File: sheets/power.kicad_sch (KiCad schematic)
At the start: 85 parts, among them Q11 C1815, Q12 A1015, Q13 A1442, T1 COIL, U11 74LS05, U12 74LS06, U28 PC4741, U29 PC4741, U33 74AS04, U37 LM2576T-5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

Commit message: Update Power Circuit 9
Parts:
- added R83: 100, 1_NeoGeoLibrary:CAP3-5mm, symbol Device:R_Small
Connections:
- net GND: now also R83.2; no longer D12.1 (K)
- net VCC: now also D12.1 (K)
- net at Q12.2 (C), Q13.1 (B): now also R83.1
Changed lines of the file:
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@@
   (junction (at 140.335 127) (diameter 0) (color 0 0 0 0)
+  )
+  (junction (at 85.09 74.93) (diameter 0) (color 0 0 0 0)
   )
   (junction (at 160.782 141.605) (diameter 0) (color 0 0 0 0)
@@
     (stroke (width 0) (type default) (color 0 0 0 0))
   )
-  (wire (pts (xy 108.966 106.68) (xy 108.966 107.569))
+  (wire (pts (xy 108.966 106.68) (xy 108.966 108.458))
     (stroke (width 0) (type default) (color 0 0 0 0))
   )
@@
     (stroke (width 0) (type default) (color 0 0 0 0))
   )
-  (wire (pts (xy 82.55 74.93) (xy 87.884 74.93))
+  (wire (pts (xy 82.55 74.93) (xy 85.09 74.93))
     (stroke (width 0) (type default) (color 0 0 0 0))
   )
@@
     (stroke (width 0) (type default) (color 0 0 0 0))
   )
+  (wire (pts (xy 85.09 74.93) (xy 87.884 74.93))
+    (stroke (width 0) (type default) (color 0 0 0 0))
+  )
   (wire (pts (xy 140.462 146.685) (xy 150.622 146.685))
     (stroke (width 0) (type default) (color 0 0 0 0))
@@
   )
   (wire (pts (xy 140.589 60.706) (xy 158.623 60.706))
+    (stroke (width 0) (type default) (color 0 0 0 0))
+  )
+  (wire (pts (xy 85.09 74.93) (xy 85.09 75.184))
     (stroke (width 0) (type default) (color 0 0 0 0))
   )
@@
     (pin "1")
   )
+  (symbol (lib_id "Device:R_Small") (at 85.09 77.724 0) (mirror y) (unit 1)
+    (in_bom yes) (on_board yes)
+    (property "Reference" "R83" (id 0) (at 88.011 76.581 0))
+    (property "Value" "100" (id 1) (at 88.011 78.867 0))
+    (property "Footprint" "1_NeoGeoLibrary:CAP3-5mm" (id 2) (at 85.09 77.724 0)
+      (effects (font (size 1.27 1.27)) hide)
+    )
+    (property "Datasheet" "~" (id 3) (at 85.09 77.724 0)
+      (effects (font (size 1.27 1.27)) hide)
+    )
+    (pin "1")
+    (pin "2")
+  )
   (symbol (lib_id "74xx:74LS04") (at 30.48 218.44 0) (unit 1)
     (in_bom yes) (on_board yes)
@@
     (pin "1")
   )
+  (symbol (lib_id "power:GND") (at 85.09 80.264 0) (unit 1)
+    (in_bom yes) (on_board yes)
+    (property "Reference" "#PWR?" (id 0) (at 85.09 86.614 0)
+      (effects (font (size 1.27 1.27)) hide)
+    )
+    (property "Value" "GND" (id 1) (at 85.09 83.82 0))
+    (property "Footprint" "" (id 2) (at 85.09 80.264 0)
+      (effects (font (size 1.27 1.27)) hide)
+    )
+    (property "Datasheet" "" (id 3) (at 85.09 80.264 0)
+      (effects (font (size 1.27 1.27)) hide)
+    )
+    (pin "1")
+  )
   (symbol (lib_id "power:GND") (at 140.589 70.866 0) (unit 1)
     (in_bom yes) (on_board yes)
@@
     )
     (property "Datasheet" "" (id 3) (at 23.368 271.78 0)
+      (effects (font (size 1.27 1.27)) hide)
+    )
+    (pin "1")
+  )
+  (symbol (lib_id "power:VCC") (at 108.966 108.458 180) (unit 1)
+    (in_bom yes) (on_board yes)
+    (property "Reference" "#PWR?" (id 0) (at 108.966 104.648 0)
+      (effects (font (size 1.27 1.27)) hide)
+    )
+    (property "Value" "VCC" (id 1) (at 108.966 112.268 0))
+    (property "Footprint" "" (id 2) (at 108.966 108.458 0)
+      (effects (font (size 1.27 1.27)) hide)
+    )
+    (property "Datasheet" "" (id 3) (at 108.966 108.458 0)
       (effects (font (size 1.27 1.27)) hide)
     )
@@
     (pin "2")
   )
-  (symbol (lib_id "power:GND") (at 108.966 107.569 0) (unit 1)
-    (in_bom yes) (on_board yes) (fields_autoplaced)
-    (property "Reference" "#PWR0279" (id 0) (at 108.966 113.919 0)
-      (effects (font (size 1.27 1.27)) hide)
-    )
-    (property "Value" "GND" (id 1) (at 108.966 112.395 0))
-    (property "Footprint" "" (id 2) (at 108.966 107.569 0)
-      (effects (font (size 1.27 1.27)) hide)
-    )
-    (property "Datasheet" "" (id 3) (at 108.966 107.569 0)
-      (effects (font (size 1.27 1.27)) hide)
-    )
-    (pin "1")
-  )
   (symbol (lib_id "74xx:74LS04") (at 30.48 187.96 0) (unit 3)

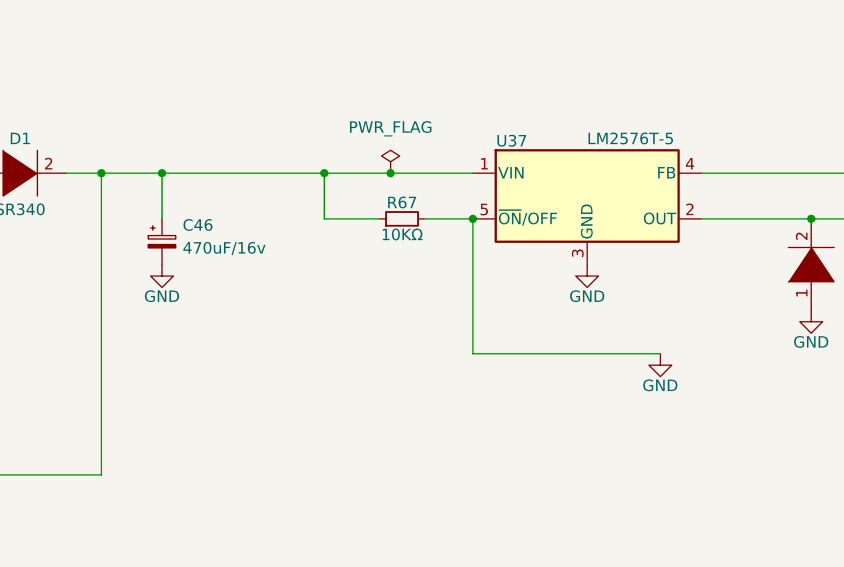
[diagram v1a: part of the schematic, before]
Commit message: Update Power Circuit 10
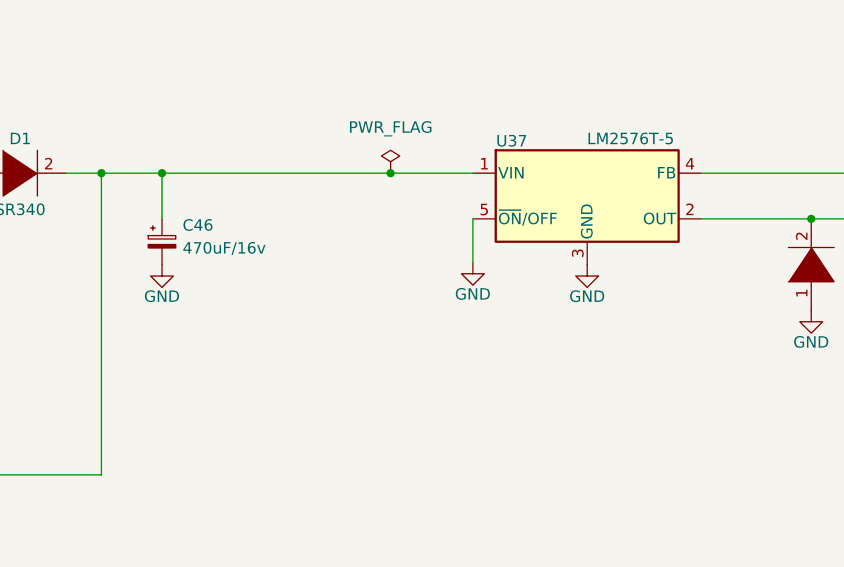
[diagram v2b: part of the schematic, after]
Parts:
- removed R67: 10KΩ, 1_NeoGeoLibrary:Resistor1-5mm, symbol Device:R_Small
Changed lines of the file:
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@@
   (junction (at 48.895 127) (diameter 0) (color 0 0 0 0)
   )
-  (junction (at 158.623 60.706) (diameter 0) (color 0 0 0 0)
-  )
   (junction (at 191.262 146.685) (diameter 0) (color 0 0 0 0)
   )
@@
   )
   (junction (at 23.368 246.38) (diameter 0) (color 0 0 0 0)
-  )
-  (junction (at 175.133 65.786) (diameter 0) (color 0 0 0 0)
   )
   (junction (at 89.535 127) (diameter 0) (color 0 0 0 0)
@@
     (stroke (width 0) (type default) (color 0 0 0 0))
   )
-  (wire (pts (xy 169.799 65.786) (xy 175.133 65.786))
-    (stroke (width 0) (type default) (color 0 0 0 0))
-  )
-  (wire (pts (xy 175.133 80.772) (xy 195.961 80.772))
-    (stroke (width 0) (type default) (color 0 0 0 0))
-  )
   (wire (pts (xy 252.222 141.605) (xy 262.382 141.605))
     (stroke (width 0) (type default) (color 0 0 0 0))
@@
     (stroke (width 0) (type default) (color 0 0 0 0))
   )
-  (wire (pts (xy 158.623 65.786) (xy 164.719 65.786))
-    (stroke (width 0) (type default) (color 0 0 0 0))
-  )
   (wire (pts (xy 59.182 146.685) (xy 69.342 146.685))
     (stroke (width 0) (type default) (color 0 0 0 0))
@@
     (stroke (width 0) (type default) (color 0 0 0 0))
   )
-  (wire (pts (xy 158.623 60.706) (xy 165.989 60.706))
-    (stroke (width 0) (type default) (color 0 0 0 0))
-  )
   (wire (pts (xy 49.022 141.605) (xy 59.182 141.605))
     (stroke (width 0) (type default) (color 0 0 0 0))
@@
     (stroke (width 0) (type default) (color 0 0 0 0))
   )
+  (wire (pts (xy 175.133 65.786) (xy 175.133 70.612))
+    (stroke (width 0) (type default) (color 0 0 0 0))
+  )
   (wire (pts (xy 22.86 218.44) (xy 22.86 223.52))
     (stroke (width 0) (type default) (color 0 0 0 0))
   )
-  (wire (pts (xy 175.133 65.786) (xy 175.133 80.772))
-    (stroke (width 0) (type default) (color 0 0 0 0))
-  )
   (wire (pts (xy 256.413 65.786) (xy 262.001 65.786))
     (stroke (width 0) (type default) (color 0 0 0 0))
@@
     (stroke (width 0) (type default) (color 0 0 0 0))
   )
-  (wire (pts (xy 158.623 60.706) (xy 158.623 65.786))
-    (stroke (width 0) (type default) (color 0 0 0 0))
-  )
   (wire (pts (xy 241.935 132.08) (xy 252.095 132.08))
     (stroke (width 0) (type default) (color 0 0 0 0))
@@
     (stroke (width 0) (type default) (color 0 0 0 0))
   )
-  (wire (pts (xy 140.589 60.706) (xy 158.623 60.706))
+  (wire (pts (xy 140.589 60.706) (xy 165.989 60.706))
     (stroke (width 0) (type default) (color 0 0 0 0))
   )
@@
     (pin "2")
   )
-  (symbol (lib_id "power:GND") (at 195.961 80.772 0) (unit 1)
-    (in_bom yes) (on_board yes)
-    (property "Reference" "#PWR0258" (id 0) (at 195.961 87.122 0)
-      (effects (font (size 1.27 1.27)) hide)
-    )
-    (property "Value" "GND" (id 1) (at 195.961 84.328 0))
-    (property "Footprint" "" (id 2) (at 195.961 80.772 0)
-      (effects (font (size 1.27 1.27)) hide)
-    )
-    (property "Datasheet" "" (id 3) (at 195.961 80.772 0)
+  (symbol (lib_id "power:GND") (at 175.133 70.612 0) (unit 1)
+    (in_bom yes) (on_board yes)
+    (property "Reference" "#PWR0258" (id 0) (at 175.133 76.962 0)
+      (effects (font (size 1.27 1.27)) hide)
+    )
+    (property "Value" "GND" (id 1) (at 175.133 74.168 0))
+    (property "Footprint" "" (id 2) (at 175.133 70.612 0)
+      (effects (font (size 1.27 1.27)) hide)
+    )
+    (property "Datasheet" "" (id 3) (at 175.133 70.612 0)
       (effects (font (size 1.27 1.27)) hide)
     )
@@
       (effects (font (size 1.27 1.27)) hide)
     )
-    (pin "1")
-    (pin "2")
-  )
-  (symbol (lib_id "Device:R_Small") (at 167.259 65.786 90) (unit 1)
-    (in_bom yes) (on_board yes)
-    (property "Reference" "R67" (id 0) (at 167.259 64.008 90))
-    (property "Value" "10KΩ" (id 1) (at 167.259 67.564 90))
-    (property "Footprint" "1_NeoGeoLibrary:Resistor1-5mm" (id 2) (at 167.259 65.786 0)
-      (effects (font (size 1.27 1.27)) hide)
-    )
-    (property "Datasheet" "" (id 3) (at 167.259 65.786 0)
-      (effects (font (size 1.27 1.27)) hide)
-    )

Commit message: Merged From Stable
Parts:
- C126: footprint 1_NeoGeoLibrary:CAP3-5mm -> 1_NeoGeoLibrary:CAP2-2.5mm
- C44, C45: footprint 1_NeoGeoLibrary:CAP1-5mm -> 1_NeoGeoLibrary:CAP3-5mm
- C46: footprint 1_NeoGeoLibrary:CAP3-5mm -> 1_NeoGeoLibrary:CAP1-5mm
- C47: footprint 1_NeoGeoLibrary:CAP3-5mm -> 1_NeoGeoLibrary:CAP4-Large
- D1, D2: footprint Diode_THT:D_A-405_P10.16mm_Horizontal -> Diode_THT:D_DO-15_P15.24mm_Horizontal
- D11, D12: footprint Diode_THT:D_A-405_P10.16mm_Horizontal -> Diode_THT:D_A-405_P7.62mm_Horizontal
- J4: footprint Jumper:SolderJumper-2_P1.3mm_Open_Pad1.0x1.5mm -> 1_NeoGeoLibrary:J4
- L3: footprint 1_NeoGeoLibrary:Resistor1-5mm -> Inductor_THT:L_Toroid_Vertical_L35.1mm_W21.1mm_P18.50mm_Vishay_TJ6
- Q11: footprint Package_TO_SOT_THT:TO-92_Inline -> Package_TO_SOT_THT:TO-92_Inline_Wide
- Q13: footprint Package_TO_SOT_THT:TO-3P-3_Vertical -> Package_TO_SOT_THT:TO-220-3_Vertical
- R77: footprint 1_NeoGeoLibrary:CAP3-5mm -> Resistor_THT:R_Axial_DIN0309_L9.0mm_D3.2mm_P25.40mm_Horizontal
- R78, R79, R80, R81, R82: footprint 1_NeoGeoLibrary:CAP3-5mm -> Resistor_THT:R_Axial_DIN0207_L6.3mm_D2.5mm_P10.16mm_Horizontal
- R83: footprint 1_NeoGeoLibrary:CAP3-5mm -> Resistor_THT:R_Axial_DIN0309_L9.0mm_D3.2mm_P20.32mm_Horizontal
- SW2: footprint Button_Switch_THT:SW_Slide_1P2T_CK_OS102011MS2Q -> 1_NeoGeoLibrary:SW2
- T1: footprint Transformer_THT:Transformer_NF_ETAL_1-1_P1200 -> 1_NeoGeoLibrary:T1
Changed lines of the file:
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@@
     (property "Reference" "J4" (id 0) (at 29.718 16.0528 90))
     (property "Value" "~" (id 1) (at 30.0736 16.1036 90))
-    (property "Footprint" "Jumper:SolderJumper-2_P1.3mm_Open_Pad1.0x1.5mm" (id 2) (at 30.734 23.622 0)
+    (property "Footprint" "1_NeoGeoLibrary:J4" (id 2) (at 30.734 23.622 0)
       (effects (font (size 1.27 1.27)) hide)
     )
@@
       (effects (font (size 1.27 1.27)) (justify left))
     )
-    (property "Footprint" "Package_TO_SOT_THT:TO-3P-3_Vertical" (id 2) (at 98.044 77.47 0)
+    (property "Footprint" "Package_TO_SOT_THT:TO-220-3_Vertical" (id 2) (at 98.044 77.47 0)
       (effects (font (size 1.27 1.27)) hide)
     )
@@
     (property "Reference" "R81" (id 0) (at 111.887 73.533 0))
     (property "Value" "100" (id 1) (at 111.887 75.819 0))
-    (property "Footprint" "1_NeoGeoLibrary:CAP3-5mm" (id 2) (at 108.966 74.676 0)
+    (property "Footprint" "Resistor_THT:R_Axial_DIN0207_L6.3mm_D2.5mm_P10.16mm_Horizontal" (id 2) (at 108.966 74.676 0)
       (effects (font (size 1.27 1.27)) hide)
     )
@@
       (effects (font (size 1.27 1.27)) (justify right))
     )
-    (property "Footprint" "Diode_THT:D_A-405_P10.16mm_Horizontal" (id 2) (at 108.966 104.14 90)
+    (property "Footprint" "Diode_THT:D_A-405_P7.62mm_Horizontal" (id 2) (at 108.966 104.14 90)
       (effects (font (size 1.27 1.27)) hide)
     )
@@
     (property "Reference" "R80" (id 0) (at 46.355 78.994 0))
     (property "Value" "470" (id 1) (at 46.355 81.28 0))
-    (property "Footprint" "1_NeoGeoLibrary:CAP3-5mm" (id 2) (at 49.276 80.137 0)
+    (property "Footprint" "Resistor_THT:R_Axial_DIN0207_L6.3mm_D2.5mm_P10.16mm_Horizontal" (id 2) (at 49.276 80.137 0)
       (effects (font (size 1.27 1.27)) hide)
     )
@@
     (property "Reference" "R83" (id 0) (at 88.011 76.581 0))
     (property "Value" "100" (id 1) (at 88.011 78.867 0))
-    (property "Footprint" "1_NeoGeoLibrary:CAP3-5mm" (id 2) (at 85.09 77.724 0)
+    (property "Footprint" "Resistor_THT:R_Axial_DIN0309_L9.0mm_D3.2mm_P20.32mm_Horizontal" (id 2) (at 85.09 77.724 0)
       (effects (font (size 1.27 1.27)) hide)
     )
@@
       (effects (font (size 1.27 1.27)) (justify left))
     )
-    (property "Footprint" "1_NeoGeoLibrary:CAP3-5mm" (id 2) (at 18.542 144.145 0)
+    (property "Footprint" "1_NeoGeoLibrary:CAP2-2.5mm" (id 2) (at 18.542 144.145 0)
       (effects (font (size 1.27 1.27)) hide)
     )
@@
     (property "Reference" "Q11" (id 0) (at 62.103 90.043 90))
     (property "Value" "C1815" (id 1) (at 62.103 92.583 90))
-    (property "Footprint" "Package_TO_SOT_THT:TO-92_Inline" (id 2) (at 54.737 84.074 0)
+    (property "Footprint" "Package_TO_SOT_THT:TO-92_Inline_Wide" (id 2) (at 54.737 84.074 0)
       (effects (font (size 1.27 1.27) italic) (justify left) hide)
     )
@@
   (symbol (lib_id "power:GND") (at 85.09 80.264 0) (unit 1)
     (in_bom yes) (on_board yes)
-    (property "Reference" "#PWR?" (id 0) (at 85.09 86.614 0)
+    (property "Reference" "#PWR0279" (id 0) (at 85.09 86.614 0)
       (effects (font (size 1.27 1.27)) hide)
     )
@@
   (symbol (lib_id "power:VCC") (at 108.966 108.458 180) (unit 1)
     (in_bom yes) (on_board yes)
-    (property "Reference" "#PWR?" (id 0) (at 108.966 104.648 0)
+    (property "Reference" "#PWR0280" (id 0) (at 108.966 104.648 0)
       (effects (font (size 1.27 1.27)) hide)
     )
@@
       (effects (font (size 1.27 1.27)) (justify left))
     )
-    (property "Footprint" "1_NeoGeoLibrary:CAP1-5mm" (id 2) (at 46.482 40.132 0)
+    (property "Footprint" "1_NeoGeoLibrary:CAP3-5mm" (id 2) (at 46.482 40.132 0)
       (effects (font (size 1.27 1.27)) hide)
     )
@@
       (effects (font (size 1.27 1.27)) (justify left))
     )
-    (property "Footprint" "1_NeoGeoLibrary:CAP3-5mm" (id 2) (at 140.589 68.326 0)
+    (property "Footprint" "1_NeoGeoLibrary:CAP1-5mm" (id 2) (at 140.589 68.326 0)
       (effects (font (size 1.27 1.27)) hide)
     )
@@
     (property "Reference" "SW2" (id 0) (at 37.846 61.722 0))
     (property "Value" "~" (id 1) (at 37.846 60.706 0))
-    (property "Footprint" "Button_Switch_THT:SW_Slide_1P2T_CK_OS102011MS2Q" (id 2) (at 37.846 65.786 0)
+    (property "Footprint" "1_NeoGeoLibrary:SW2" (id 2) (at 37.846 65.786 0)
       (effects (font (size 1.27 1.27)) hide)
     )
@@
     (property "Reference" "R78" (id 0) (at 54.483 78.994 0))
     (property "Value" "1K" (id 1) (at 54.483 81.28 0))
-    (property "Footprint" "1_NeoGeoLibrary:CAP3-5mm" (id 2) (at 51.562 80.137 0)
+    (property "Footprint" "Resistor_THT:R_Axial_DIN0207_L6.3mm_D2.5mm_P10.16mm_Horizontal" (id 2) (at 51.562 80.137 0)
       (effects (font (size 1.27 1.27)) hide)
     )
@@
     (property "Reference" "R77" (id 0) (at 69.596 69.85 90))
     (property "Value" "10K" (id 1) (at 69.596 67.564 90))
-    (property "Footprint" "1_NeoGeoLibrary:CAP3-5mm" (id 2) (at 69.596 65.786 0)
+    (property "Footprint" "Resistor_THT:R_Axial_DIN0309_L9.0mm_D3.2mm_P25.40mm_Horizontal" (id 2) (at 69.596 65.786 0)
       (effects (font (size 1.27 1.27)) hide)
     )
@@
     (property "Reference" "D2" (id 0) (at 217.551 69.596 90))
     (property "Value" "SR340" (id 1) (at 219.329 72.39 90))
-    (property "Footprint" "Diode_THT:D_A-405_P10.16mm_Horizontal" (id 2) (at 212.725 70.866 0)
+    (property "Footprint" "Diode_THT:D_DO-15_P15.24mm_Horizontal" (id 2) (at 212.725 70.866 0)
       (effects (font (size 1.27 1.27)) hide)
     )
@@
     (property "Reference" "D1" (id 0) (at 124.841 56.896 0))
     (property "Value" "SR340" (id 1) (at 124.841 64.77 0))
-    (property "Footprint" "Diode_THT:D_A-405_P10.16mm_Horizontal" (id 2) (at 124.841 60.706 0)
+    (property "Footprint" "Diode_THT:D_DO-15_P15.24mm_Horizontal" (id 2) (at 124.841 60.706 0)
       (effects (font (size 1.27 1.27)) hide)
     )
@@
     (property "Reference" "R79" (id 0) (at 68.58 82.55 90))
     (property "Value" "510" (id 1) (at 68.58 84.836 90))
-    (property "Footprint" "1_NeoGeoLibrary:CAP3-5mm" (id 2) (at 68.58 86.614 0)
+    (property "Footprint" "Resistor_THT:R_Axial_DIN0207_L6.3mm_D2.5mm_P10.16mm_Horizontal" (id 2) (at 68.58 86.614 0)
       (effects (font (size 1.27 1.27)) hide)
     )
@@
       (effects (font (size 1.27 1.27)) (justify left))
     )
-    (property "Footprint" "1_NeoGeoLibrary:CAP1-5mm" (id 2) (at 93.218 40.132 0)
+    (property "Footprint" "1_NeoGeoLibrary:CAP3-5mm" (id 2) (at 93.218 40.132 0)
       (effects (font (size 1.27 1.27)) hide)
     )
@@
     (property "Reference" "R82" (id 0) (at 111.887 89.916 0))
     (property "Value" "510" (id 1) (at 111.887 92.202 0))
-    (property "Footprint" "1_NeoGeoLibrary:CAP3-5mm" (id 2) (at 108.966 91.059 0)
+    (property "Footprint" "Resistor_THT:R_Axial_DIN0207_L6.3mm_D2.5mm_P10.16mm_Horizontal" (id 2) (at 108.966 91.059 0)
       (effects (font (size 1.27 1.27)) hide)
     )
@@
     (property "Reference" "L3" (id 0) (at 236.093 63.754 90))
     (property "Value" "180uH" (id 1) (at 236.093 67.31 90))
-    (property "Footprint" "1_NeoGeoLibrary:Resistor1-5mm" (id 2) (at 236.093 65.786 0)
+    (property "Footprint" "Inductor_THT:L_Toroid_Vertical_L35.1mm_W21.1mm_P18.50mm_Vishay_TJ6" (id 2) (at 236.093 65.786 0)
       (effects (font (size 1.27 1.27)) hide)
     )
@@
       (effects (font (size 1.27 1.27)) (justify right))
     )
-    (property "Footprint" "Transformer_THT:Transformer_NF_ETAL_1-1_P1200" (id 2) (at 69.85 40.132 0)
+    (property "Footprint" "1_NeoGeoLibrary:T1" (id 2) (at 69.85 40.132 0)
       (effects (font (size 1.27 1.27)) hide)
     )
@@
       (effects (font (size 1.27 1.27)) (justify left))
     )
-    (property "Footprint" "1_NeoGeoLibrary:CAP3-5mm" (id 2) (at 251.333 73.406 0)
+    (property "Footprint" "1_NeoGeoLibrary:CAP4-Large" (id 2) (at 251.333 73.406 0)
       (effects (font (size 1.27 1.27)) hide)
     )
@@
       (effects (font (size 1.27 1.27)) (justify right))
     )
-    (property "Footprint" "Diode_THT:D_A-405_P10.16mm_Horizontal" (id 2) (at 108.966 97.536 90)
-      (effects (font (size 1.27 1.27)) hide)
-    )
+    (property "Footprint" "Diode_THT:D_A-405_P7.62mm_Horizontal" (id 2) (at 108.966 97.536 90)
+      (effects (font (size 1.27 1.27)) hide)
+    )
